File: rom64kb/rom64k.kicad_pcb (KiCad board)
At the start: 2 copper layers, 81.3 x 65.3 mm, 3 parts, among them P1 CONN_02X25, U2 SST39SF010

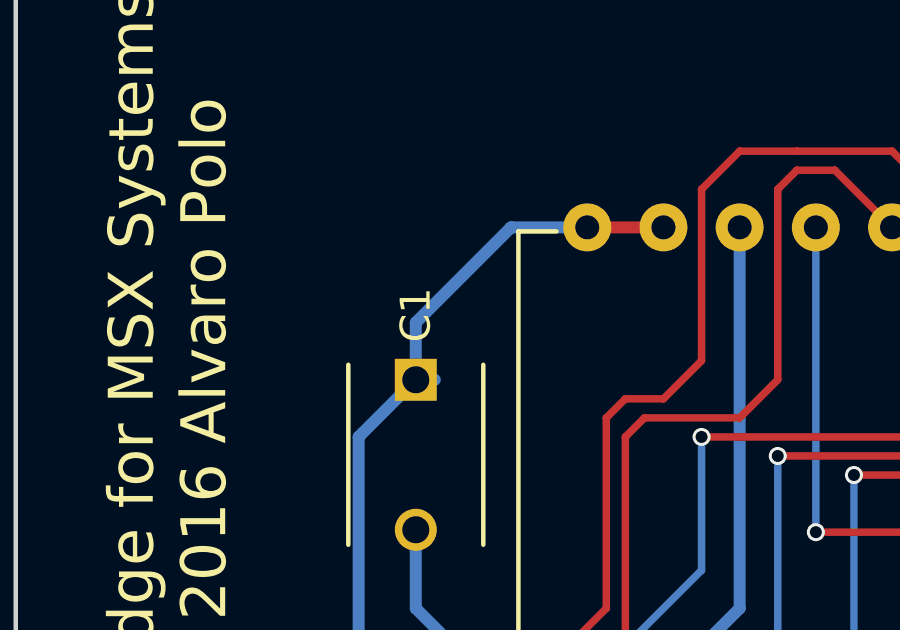
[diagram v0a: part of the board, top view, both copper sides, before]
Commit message: [rom64] Adapt the design to KiCAD 6
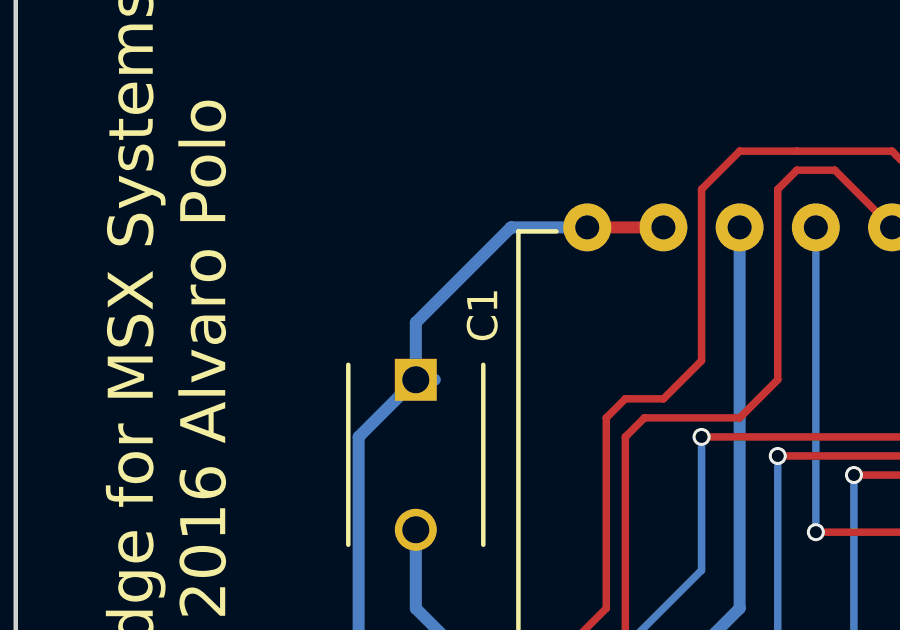
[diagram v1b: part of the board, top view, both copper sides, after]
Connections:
- net ~RD renamed ~{RD}
- net ~SLTSL renamed ~{SLTSL}
- P1 pad 1: (no net) -> unconnected-(P1-Pad1)
- P1 pad 10: (no net) -> unconnected-(P1-Pad10)
- P1 pad 11: (no net) -> unconnected-(P1-Pad11)
- P1 pad 12: (no net) -> unconnected-(P1-Pad12)
- P1 pad 13: (no net) -> unconnected-(P1-Pad13)
- P1 pad 15: (no net) -> unconnected-(P1-Pad15)
- P1 pad 16: (no net) -> unconnected-(P1-Pad16)
- P1 pad 2: (no net) -> unconnected-(P1-Pad2)
- P1 pad 3: (no net) -> unconnected-(P1-Pad3)
- P1 pad 42: (no net) -> unconnected-(P1-Pad42)
- P1 pad 48: (no net) -> unconnected-(P1-Pad48)
- P1 pad 49: (no net) -> unconnected-(P1-Pad49)
- P1 pad 5: (no net) -> unconnected-(P1-Pad5)
- P1 pad 50: (no net) -> unconnected-(P1-Pad50)
- P1 pad 6: (no net) -> unconnected-(P1-Pad6)
- P1 pad 7: (no net) -> unconnected-(P1-Pad7)
- P1 pad 8: (no net) -> unconnected-(P1-Pad8)
- P1 pad 9: (no net) -> unconnected-(P1-Pad9)
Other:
- net class Default removed
- net class Power removed
